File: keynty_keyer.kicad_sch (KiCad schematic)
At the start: 32 parts, among them J1 Key Input, J2 Conn_01x03, J3 Conn_01x03, J4 Key Input, Q1 ZXM61N02FTC, SW1 Power, SW2 IAMBIC Mode, SW3 Sidetone Enable, U1 4081, U2 4071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

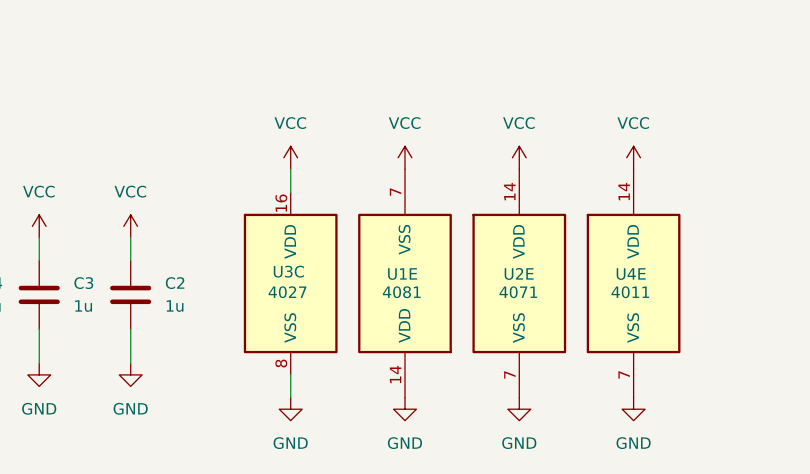
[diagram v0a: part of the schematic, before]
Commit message: correct powwer supply inverted
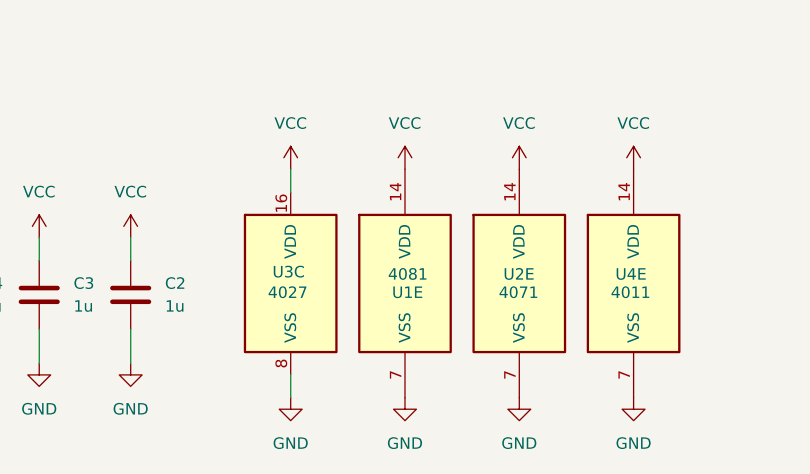
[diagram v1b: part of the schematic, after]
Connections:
- net GND: now also U1.7 (VSS); no longer U1.14 (VDD)
- net VCC: now also U1.14 (VDD); no longer U1.7 (VSS)
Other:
- moved on the sheet: U1E
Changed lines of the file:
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@@
 	(symbol
 		(lib_id "4xxx:4081")
-		(at 143.51 173.99 180)
+		(at 143.51 173.99 0)
 		(unit 5)
 		(body_style 1)
@@
 		(dnp no)
 		(property "Reference" "U1"
-			(at 141.478 172.974 0)
+			(at 145.542 175.006 0)
 			(show_name no)
 			(do_not_autoplace no)
@@
 		)
 		(property "Value" "4081"
-			(at 140.97 175.006 0)
+			(at 146.05 172.974 0)
 			(show_name no)
 			(do_not_autoplace no)

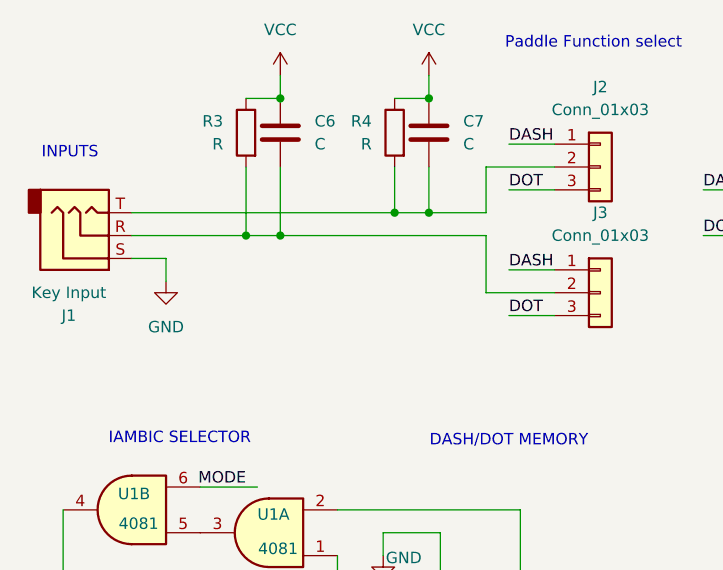
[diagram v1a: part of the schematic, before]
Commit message: changed pull down ok the inputs
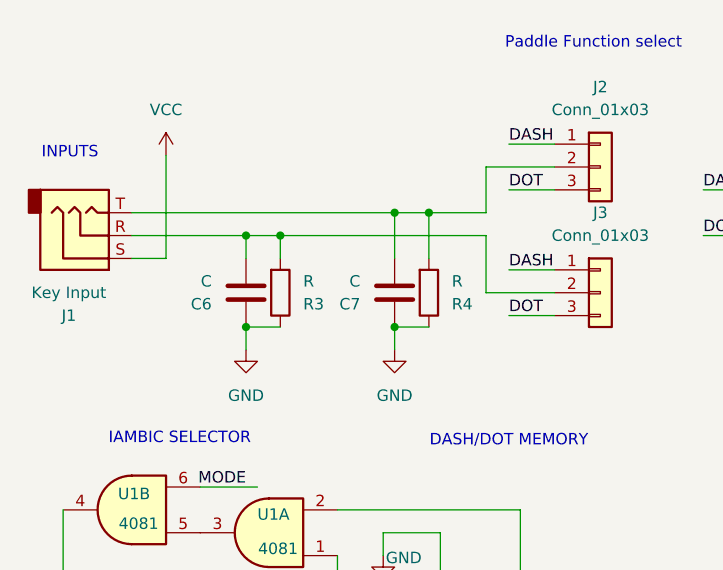
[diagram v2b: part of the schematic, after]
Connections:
- net GND: now also C6.1, C7.1, R3.1, R4.1; no longer J1.S
- net VCC: now also J1.S; no longer C6.1, C7.1, R3.1, R4.1
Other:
- moved on the sheet: C6, C7, R3, R4

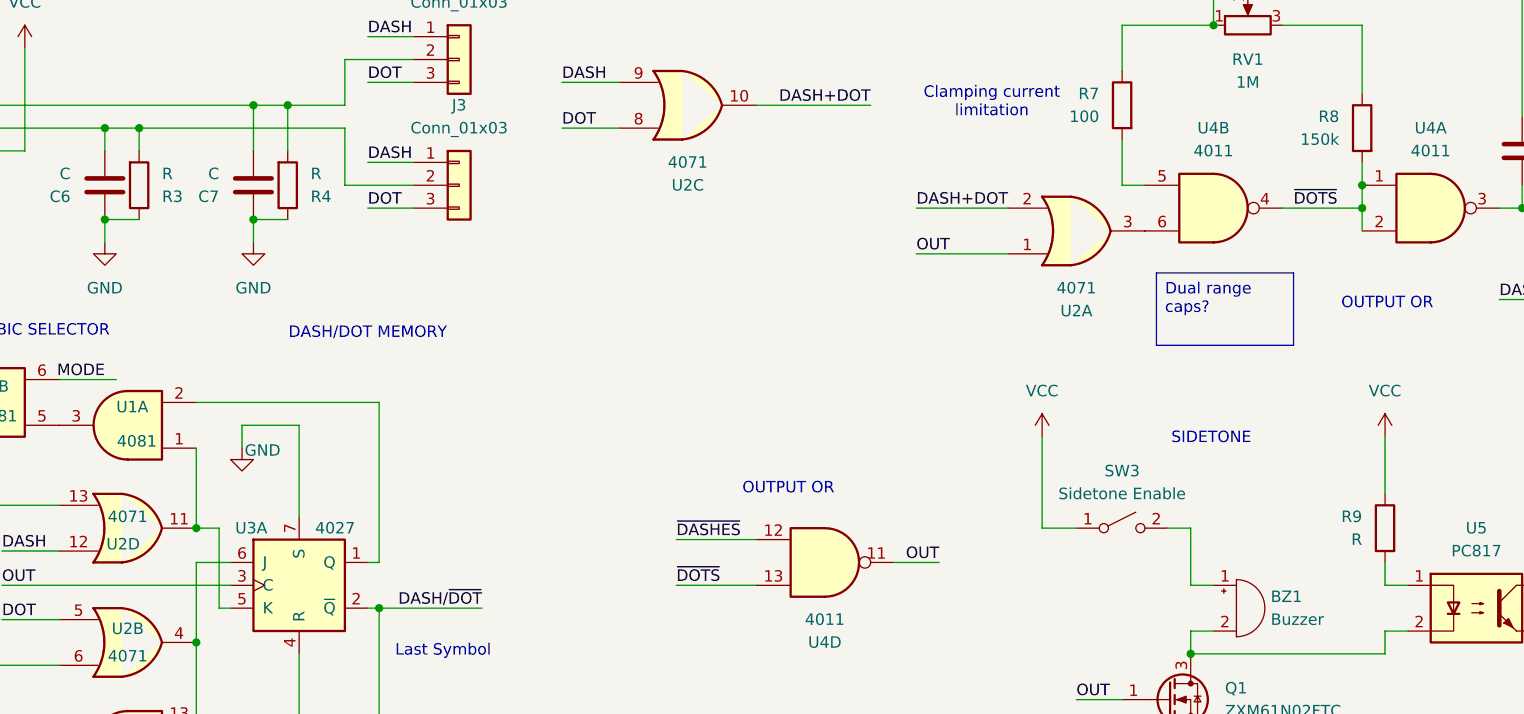
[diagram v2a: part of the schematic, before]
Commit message: added missing resistor values for pull-down and opto drive
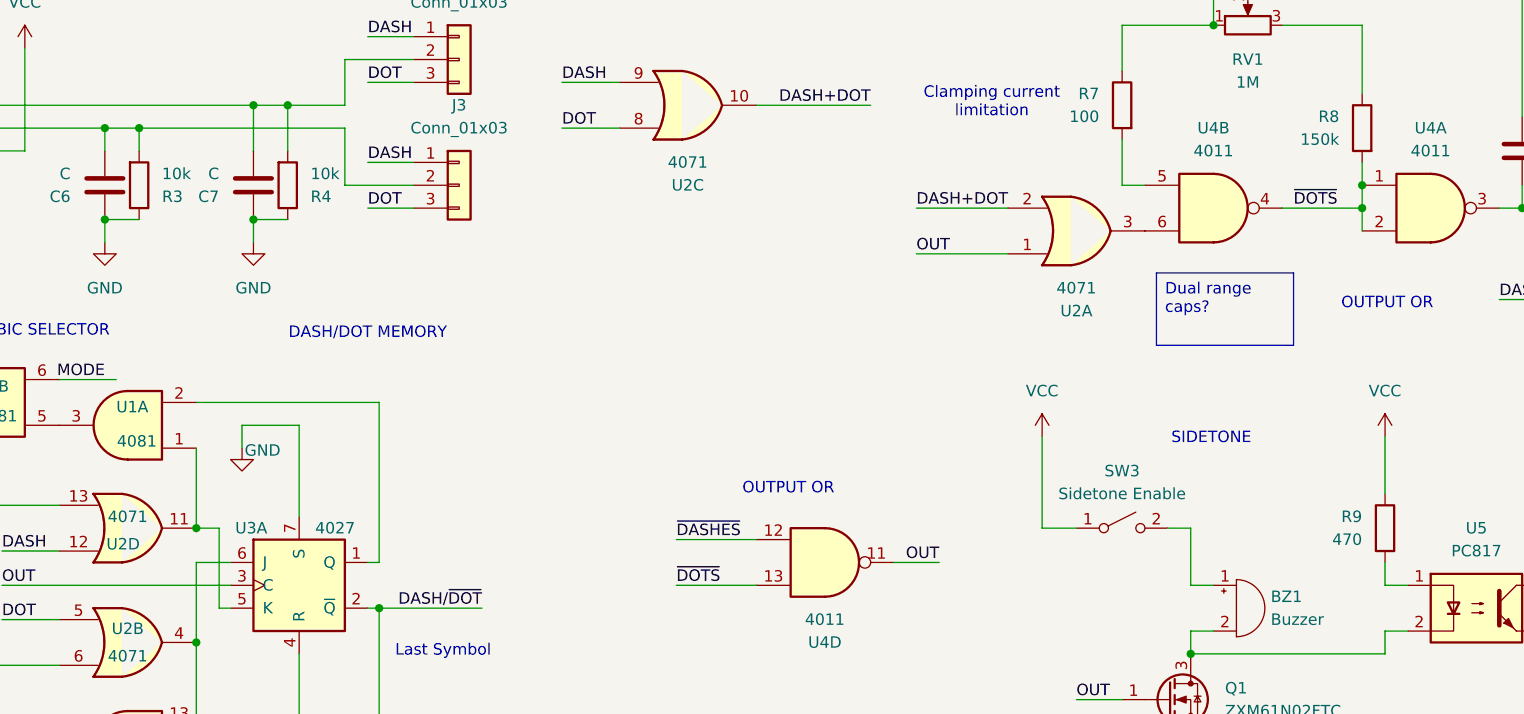
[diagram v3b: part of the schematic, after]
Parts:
- R3, R4: value R -> 10k
- R9: value R -> 470
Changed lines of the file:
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@@
 			)
 		)
-		(property "Value" "R"
+		(property "Value" "10k"
 			(at 44.45 43.1801 0)
 			(show_name no)
@@
 			)
 		)
-		(property "Value" "R"
+		(property "Value" "470"
 			(at 177.8 83.8199 0)
 			(show_name no)
@@
 			)
 		)
-		(property "Value" "R"
+		(property "Value" "10k"
 			(at 60.96 43.1801 0)
 			(show_name no)

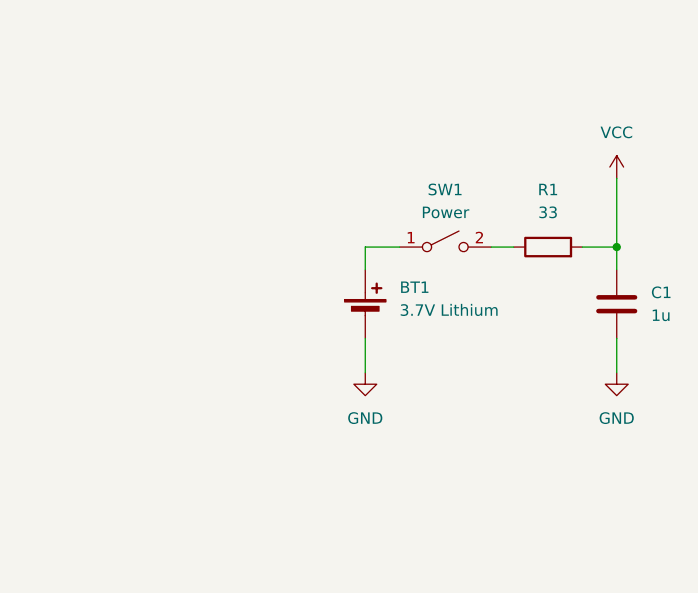
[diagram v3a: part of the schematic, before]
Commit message: corrected battery footprint, added QR, changed minor silkscreen
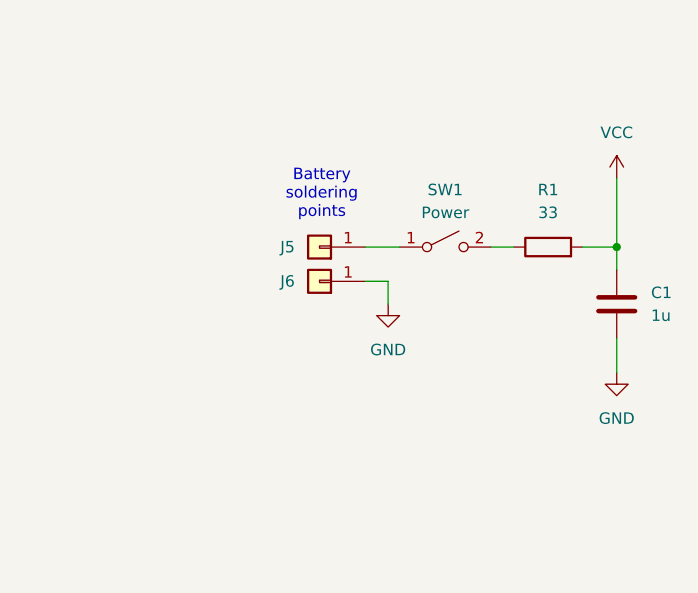
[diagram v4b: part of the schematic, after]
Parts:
- removed BT1: 3.7V Lithium, Battery:BatteryHolder_Keystone_2462_2xAA, symbol Device:Battery_Cell
- added J5, J6: Conn_01x01, TestPoint:TestPoint_THTPad_2.0x2.0mm_Drill1.0mm, symbol Connector_Generic:Conn_01x01
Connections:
- net GND: now also J6.1 (Pin_1)
- net at SW1.1 (A): now also J5.1 (Pin_1)
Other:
- note added: "Battery soldering points"
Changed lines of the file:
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@@
 		)
 	)
+	(text "Battery\nsoldering\npoints"
+		(exclude_from_sim no)
+		(at 245.364 138.938 0)
+		(effects
+			(font
+				(size 1.27 1.27)
+			)
+		)
+	)
 	(text "OUTPUT OR"
 		(exclude_from_sim no)
@@
 	(wire
 		(pts
-			(xy 250.19 154.94) (xy 250.19 158.75)
+			(xy 252.73 148.59) (xy 252.73 151.13)
 		)
 		(stroke
@@
 	(wire
 		(pts
+			(xy 252.73 148.59) (xy 250.19 148.59)
+		)
+		(stroke
+			(width 0)
+			(type default)
+		)
+	)
+	(wire
+		(pts
 			(xy 130.81 161.29) (xy 130.81 163.83)
 		)
@@
 	(wire
 		(pts
-			(xy 250.19 144.78) (xy 250.19 147.32)
-		)
-		(stroke
-			(width 0)
-			(type default)
-		)
-	)
-	(wire
-		(pts
 			(xy 53.34 71.12) (xy 59.69 71.12)
 		)
@@
 	)
 	(symbol
+		(lib_id "Connector_Generic:Conn_01x01")
+		(at 245.11 144.78 180)
+		(unit 1)
+		(body_style 1)
+		(exclude_from_sim no)
+		(in_bom yes)
+		(on_board yes)
+		(in_pos_files yes)
+		(dnp no)
+		(property "Reference" "J5"
+			(at 241.554 144.78 0)
+			(show_name no)
+			(do_not_autoplace no)
+			(effects
+				(font
+					(size 1.27 1.27)
+				)
+			)
+		)
+		(property "Value" "Conn_01x01"
+			(at 245.11 140.97 0)
+			(hide yes)
+			(show_name no)
+			(do_not_autoplace no)
+			(effects
+				(font
+					(size 1.27 1.27)
+				)
+			)
+		)
+		(property "Footprint" "TestPoint:TestPoint_THTPad_2.0x2.0mm_Drill1.0mm"
+			(at 245.11 144.78 0)
+			(hide yes)
+			(show_name no)
+			(do_not_autoplace no)
+			(effects
+				(font
+					(size 1.27 1.27)
+				)
+			)
+		)
+		(property "Datasheet" ""
+			(at 245.11 144.78 0)
+			(hide yes)
+			(show_name no)
+			(do_not_autoplace no)
+			(effects
+				(font
+					(size 1.27 1.27)
+				)
+			)
+		)
+		(property "Description" "Generic connector, single row, 01x01, script generated (kicad-library-utils/schlib/autogen/connector/)"
+			(at 245.11 144.78 0)
+			(hide yes)
+			(show_name no)
+			(do_not_autoplace no)
+			(effects
+				(font
+					(size 1.27 1.27)
+				)
+			)
+		)
+		(pin "1"
+		)
+		(instances
+			(project "keynty_keyer"
+				(path "/431ac31e-71d2-4327-97a9-de415a92d53b"
+					(reference "J5")
+					(unit 1)
+				)
+			)
+		)
+	)
+	(symbol
 		(lib_id "4xxx:4027")
 		(at 59.69 88.9 0)
@@
 	)
 	(symbol
-		(lib_id "Device:Battery_Cell")
-		(at 250.19 152.4 0)
-		(unit 1)
-		(body_style 1)
-		(exclude_from_sim no)
-		(in_bom yes)
-		(on_board yes)
-		(in_pos_files yes)
-		(dnp no)
-		(fields_autoplaced yes)
-		(property "Reference" "BT1"
-			(at 254 149.2884 0)
-			(show_name no)
-			(do_not_autoplace no)
-			(effects
-				(font
-					(size 1.27 1.27)
-				)
-				(justify left)
-			)
-		)
-		(property "Value" "3.7V Lithium"
-			(at 254 151.8284 0)
-			(show_name no)
-			(do_not_autoplace no)
-			(effects
-				(font
-					(size 1.27 1.27)
-				)
-				(justify left)
-			)
-		)
-		(property "Footprint" "Battery:BatteryHolder_Keystone_2462_2xAA"
-			(at 250.19 150.876 90)
-			(hide yes)
-			(show_name no)
-			(do_not_autoplace no)
-			(effects
-				(font
-					(size 1.27 1.27)
-				)
-			)
-		)
-		(property "Datasheet" ""
-			(at 250.19 150.876 90)
-			(hide yes)
-			(show_name no)
-			(do_not_autoplace no)
-			(effects
-				(font
-					(size 1.27 1.27)
-				)
-			)
-		)
-		(property "Description" "Single-cell battery"
-			(at 250.19 152.4 0)
-			(hide yes)
-			(show_name no)
-			(do_not_autoplace no)
-			(effects
-				(font
-					(size 1.27 1.27)
-				)
-			)
-		)
-		(property "Sim.Device" "V"
-			(at 250.19 152.4 0)
-			(hide yes)
-			(show_name no)
-			(do_not_autoplace no)
-			(effects
-				(font
-					(size 1.27 1.27)
-				)
-			)
-		)
-		(property "Sim.Type" "DC"
-			(at 250.19 152.4 0)
-			(hide yes)
-			(show_name no)
-			(do_not_autoplace no)
-			(effects
-				(font
-					(size 1.27 1.27)
-				)
-			)
-		)
-		(property "Sim.Pins" "1=+ 2=-"
-			(at 250.19 152.4 0)
-			(hide yes)
-			(show_name no)
-			(do_not_autoplace no)
-			(effects
-				(font
-					(size 1.27 1.27)
-				)
-			)
-		)
-		(pin "1"
-		)
-		(pin "2"
-		)
-		(instances
-			(project "keynty_keyer"
-				(path "/431ac31e-71d2-4327-97a9-de415a92d53b"
-					(reference "BT1")
-					(unit 1)
-				)
-			)
-		)
-	)
-	(symbol
 		(lib_id "4xxx:4081")
 		(at 25.4 68.58 180)
@@
 	(symbol
 		(lib_id "power:GND")
-		(at 250.19 158.75 0)
+		(at 252.73 151.13 0)
 		(unit 1)
 		(body_style 1)
@@
 		(fields_autoplaced yes)
 		(property "Reference" "#PWR01"
-			(at 250.19 165.1 0)
+			(at 252.73 157.48 0)
 			(hide yes)
 			(show_name no)
@@
 		)
 		(property "Value" "GND"
-			(at 250.19 163.83 0)
+			(at 252.73 156.21 0)
 			(show_name no)
 			(do_not_autoplace no)
@@
 		)
 		(property "Footprint" ""
-			(at 250.19 158.75 0)
+			(at 252.73 151.13 0)
 			(hide yes)
 			(show_name no)
@@
 		)
 		(property "Datasheet" ""
-			(at 250.19 158.75 0)
+			(at 252.73 151.13 0)
 			(hide yes)
 			(show_name no)
@@
 		)
 		(property "Description" "Power symbol creates a global label with name \"GND\" , ground"
-			(at 250.19 158.75 0)
+			(at 252.73 151.13 0)
 			(hide yes)
 			(show_name no)
@@
 					(unit 1)
 				)
+			)
+		)
+	)
+	(symbol
+		(lib_id "Connector_Generic:Conn_01x01")
+		(at 245.11 148.59 180)
+		(unit 1)
+		(body_style 1)
+		(exclude_from_sim no)
+		(in_bom yes)
+		(on_board yes)
+		(in_pos_files yes)
+		(dnp no)
+		(property "Reference" "J6"
+			(at 241.554 148.59 0)
+			(show_name no)
+			(do_not_autoplace no)
+			(effects
+				(font
+					(size 1.27 1.27)
+				)
+			)
+		)
+		(property "Value" "Conn_01x01"
+			(at 245.11 144.78 0)
+			(hide yes)
+			(show_name no)
+			(do_not_autoplace no)
+			(effects
+				(font
+					(size 1.27 1.27)
+				)
+			)
+		)
+		(property "Footprint" "TestPoint:TestPoint_THTPad_2.0x2.0mm_Drill1.0mm"
+			(at 245.11 148.59 0)
+			(hide yes)
+			(show_name no)
+			(do_not_autoplace no)
+			(effects
+				(font
+					(size 1.27 1.27)
+				)
+			)
+		)
+		(property "Datasheet" ""
+			(at 245.11 148.59 0)
+			(hide yes)
+			(show_name no)
+			(do_not_autoplace no)
+			(effects
+				(font
+					(size 1.27 1.27)
+				)
+			)
+		)
+		(property "Description" "Generic connector, single row, 01x01, script generated (kicad-library-utils/schlib/autogen/connector/)"
+			(at 245.11 148.59 0)
+			(hide yes)
+			(show_name no)
+			(do_not_autoplace no)
+			(effects
+				(font
+					(size 1.27 1.27)
+				)
+			)
+		)
+		(pin "1"
+		)
+		(instances
+			(project "keynty_keyer"
+				(path "/431ac31e-71d2-4327-97a9-de415a92d53b"
+					(reference "J6")
+					(unit 1)
+				)
